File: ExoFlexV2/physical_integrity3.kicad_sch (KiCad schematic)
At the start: 15 parts

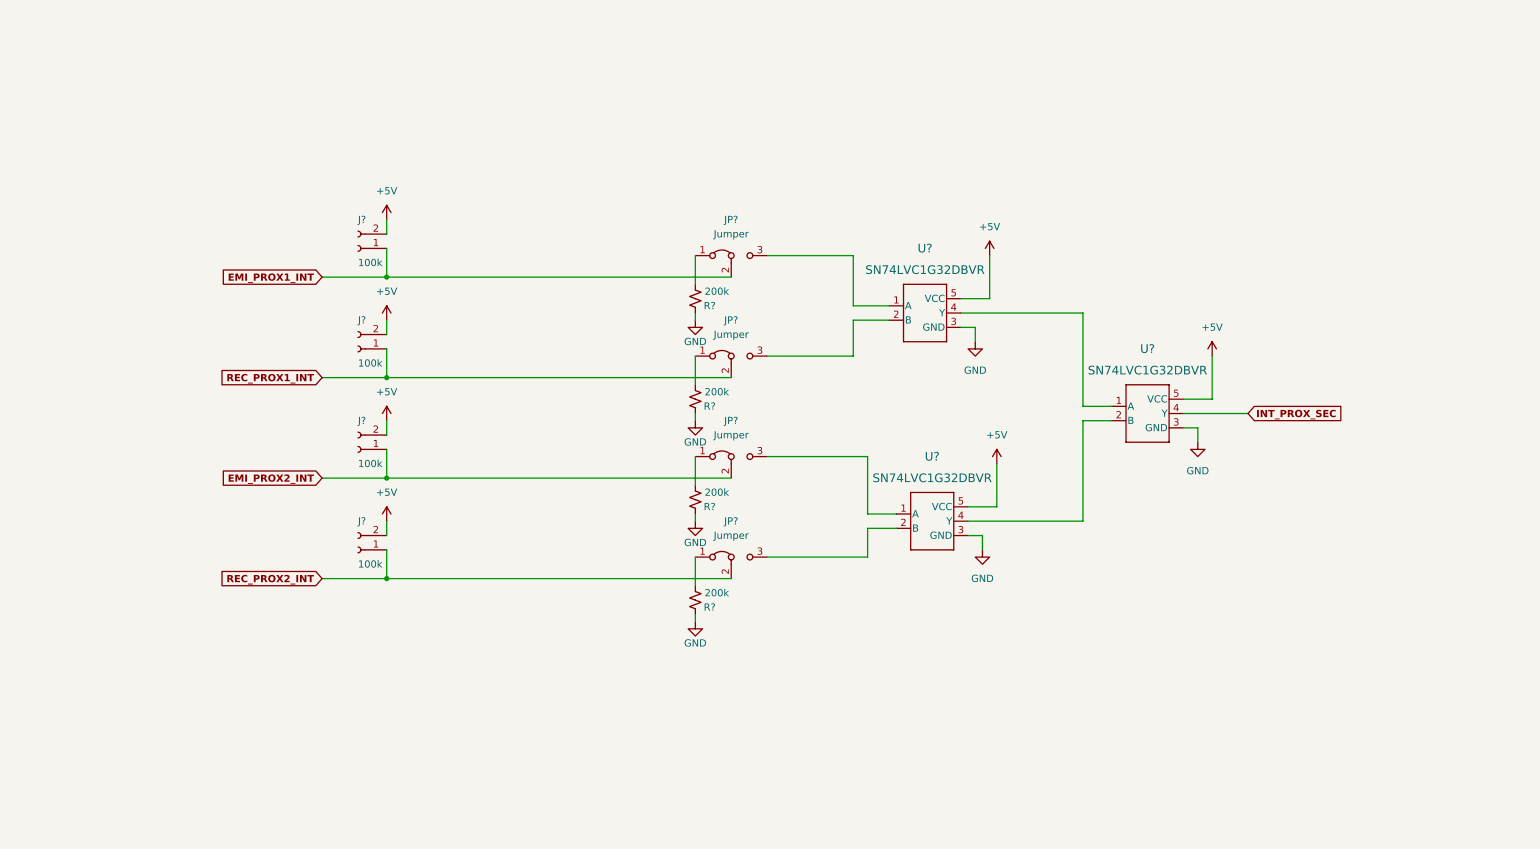
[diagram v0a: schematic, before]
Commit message: Mise à jour signaux STM
- Condo de découplage
- Signaux supplémentaire pour le STM
- Page GND sera pour Multiplexeur
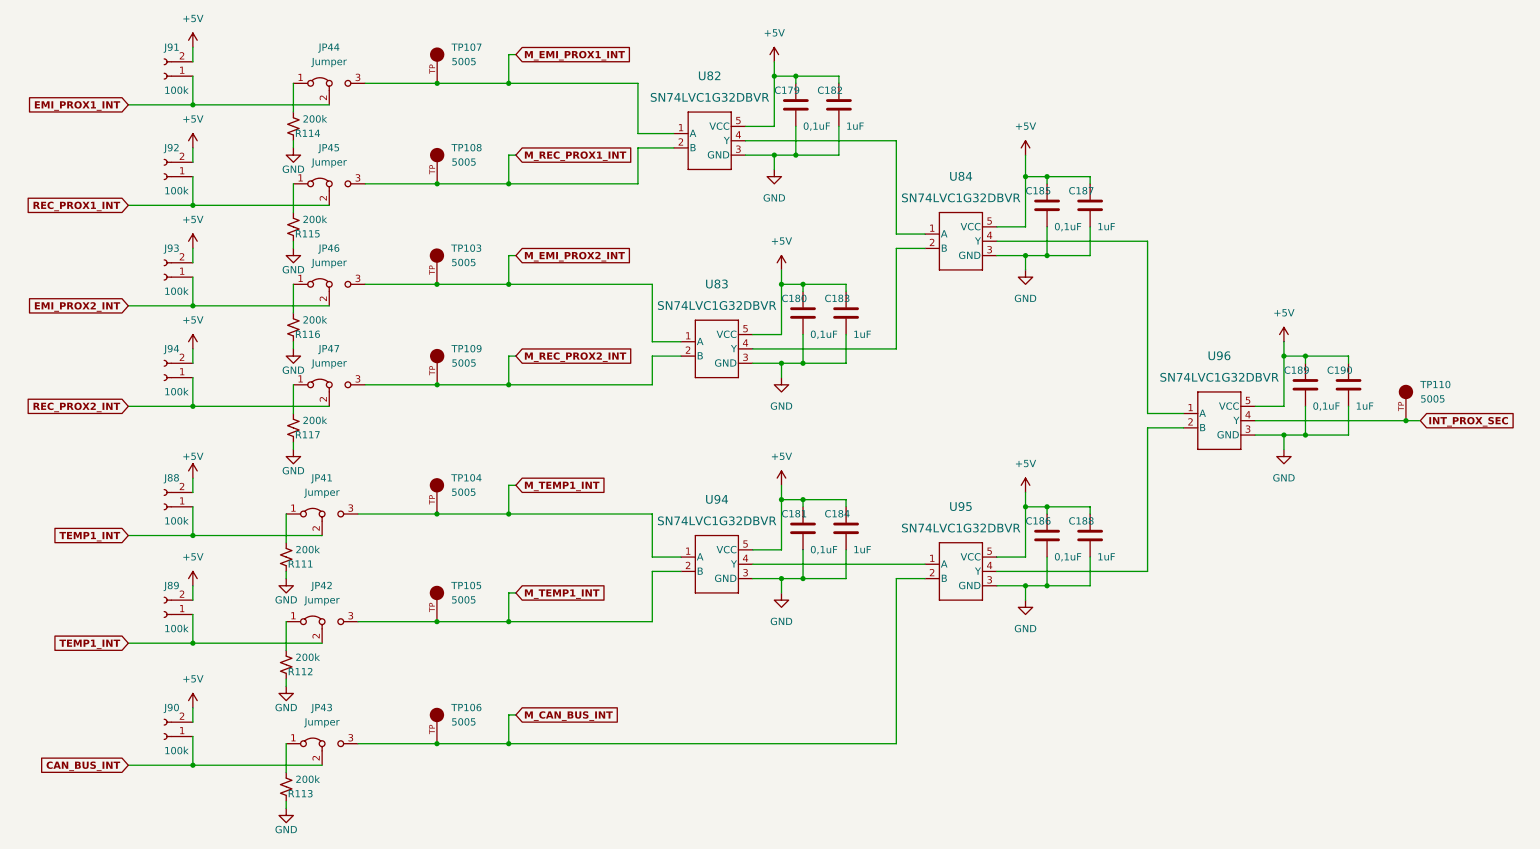
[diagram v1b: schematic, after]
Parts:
- added C179, C180, C181, C185, C186, C189: 0,1uF, Capacitor_SMD:C_0603_1608Metric, symbol Device:C
- added C182, C183, C184, C187, C188, C190: 1uF, Capacitor_SMD:C_0603_1608Metric, symbol Device:C
- added J88, J89, J90: 100k, Connector_PinHeader_2.54mm:PinHeader_1x02_P2.54mm_Vertical, symbol Connector:Conn_01x02_Female
- added JP41, JP42, JP43: Jumper, Connector_PinHeader_2.54mm:PinHeader_1x03_P2.54mm_Vertical, symbol Jumper:Jumper_3_Bridged12
- added R111, R112, R113: 200k, Resistor_SMD:R_0603_1608Metric, symbol Device:R_Small_US
- added TP103, TP104, TP105, TP106, TP107, TP108, TP109, TP110: 5005, FootPrint:KEYSTONE_5005, symbol SymLib:5005
- added U94, U95, U96: SN74LVC1G32DBVR, FootPrint:SOT95P270X145-5N, symbol SymLib:SN74LVC1G32DBVR
- gave numbers to parts that had none: 15
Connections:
- net +5V: now also C179.1, C180.1, C181.1, C182.1, C183.1, C184.1, C185.1, C186.1, C187.1, C188.1, C189.1, C190.1, J88.2 (Pin_2), J89.2 (Pin_2), J90.2 (Pin_2), U94.5 (VCC), U95.5 (VCC), U96.5 (VCC)
- net GND: now also C179.2, C180.2, C181.2, C182.2, C183.2, C184.2, C185.2, C186.2, C187.2, C188.2, C189.2, C190.2, R111.2, R112.2, R113.2, U94.3 (GND), U95.3 (GND), U96.3 (GND)
- net INT_PROX_SEC: now also TP110.TP, U96.4 (Y); no longer U84.4 (Y)
- net M_REC_PROX1_INT: now reaches JP45.3 (B), U82.2 (B)
- net M_REC_PROX1_INT: now also TP108.TP
- net M_EMI_PROX1_INT: now reaches JP44.3 (B), U82.1 (A)
- net M_EMI_PROX1_INT: now also TP107.TP
- net M_EMI_PROX2_INT: now reaches JP46.3 (B), U83.1 (A)
- net M_EMI_PROX2_INT: now also TP103.TP
- net M_REC_PROX2_INT: now reaches JP47.3 (B), U83.2 (B)
- net M_REC_PROX2_INT: now also TP109.TP
- new net: JP41.1 (A), R111.1
- new net: U94.4 (Y), U95.1 (A)
- new net: U95.4 (Y), U96.2 (B)
- new net: U84.4 (Y), U96.1 (A)
- new net: JP43.1 (A), R113.1
- new net: JP42.1 (A), R112.1
- new net CAN_BUS_INT: J90.1 (Pin_1), JP43.2 (C)
- new net M_CAN_BUS_INT: JP43.3 (B), TP106.TP, U95.2 (B)
- new net M_TEMP1_INT: JP41.3 (B), JP42.3 (B), TP104.TP, TP105.TP, U94.1 (A), U94.2 (B)
- new net TEMP1_INT: J88.1 (Pin_1), J89.1 (Pin_1), JP41.2 (C), JP42.2 (C)
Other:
- moved on the sheet: J91, J92, J93, J94, JP44, JP45, JP46, JP47, R114, R115, R116, R117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

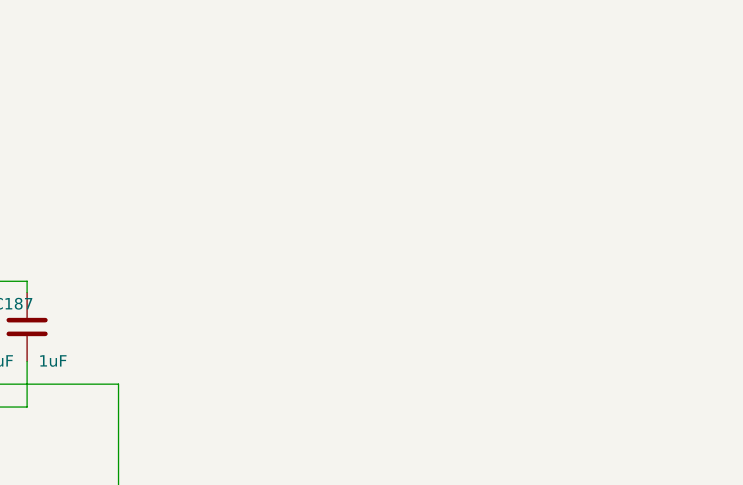
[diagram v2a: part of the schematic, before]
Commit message: Finalisation 1
- Ajout de pages pour la gestion des signaux négatif
- Modification des pages de torque et amplitude
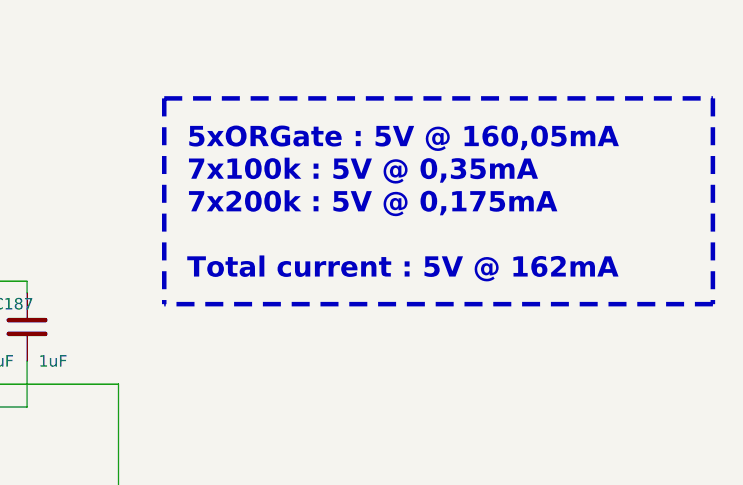
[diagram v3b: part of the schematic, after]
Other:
- note added: "5xORGate : 5V @ 160,05mA 7x100k : 5V @ 0,35mA 7x200k : 5V @ 0,175mA Total current : 5V @ 162mA"
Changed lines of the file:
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@@
     (stroke (width 0) (type default) (color 0 0 0 0))
+  )
+  (polyline (pts (xy 220.98 34.29) (xy 220.98 57.15))
+    (stroke (width 0.5) (type dash) (color 255 148 44 1))
   )
   (wire (pts (xy 205.74 113.03) (xy 198.12 113.03))
@@
     (stroke (width 0) (type default) (color 0 0 0 0))
   )
+  (polyline (pts (xy 281.94 34.29) (xy 281.94 57.15))
+    (stroke (width 0.5) (type dash) (color 255 148 44 1))
+  )
   (wire (pts (xy 153.67 45.72) (xy 153.67 50.8))
     (stroke (width 0) (type default) (color 0 0 0 0))
@@
     (stroke (width 0) (type default) (color 0 0 0 0))
   )
+  (polyline (pts (xy 220.98 34.29) (xy 281.94 34.29))
+    (stroke (width 0.5) (type dash) (color 255 148 44 1))
+  )
   (wire (pts (xy 149.86 36.83) (xy 153.67 36.83))
     (stroke (width 0) (type default) (color 0 0 0 0))
@@
     (stroke (width 0) (type default) (color 0 0 0 0))
   )
+  (polyline (pts (xy 281.94 57.15) (xy 220.98 57.15))
+    (stroke (width 0.5) (type dash) (color 255 148 44 1))
+  )
   (wire (pts (xy 102.87 149.86) (xy 102.87 154.94))
     (stroke (width 0) (type default) (color 0 0 0 0))
@@
     (stroke (width 0) (type default) (color 0 0 0 0))
   )
+  (text "5xORGate : 5V @ 160,05mA\n7x100k : 5V @ 0,35mA\n7x200k : 5V @ 0,175mA\n\nTotal current : 5V @ 162mA"
+    (at 223.52 54.61 0)
+    (effects (font (size 2.25 2.25) (thickness 0.5) bold) (justify left bottom))
+  )
   (global_label "M_CAN_BUS_INT" (shape input) (at 104.14 149.86 0) (fields_autoplaced)
